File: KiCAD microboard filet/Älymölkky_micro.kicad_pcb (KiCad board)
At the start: 2 copper layers, 36.1 x 21.1 mm, 30 parts, among them U1 nRF52810-QCxx, X1 32MHz Crystal, X1_C1 12pF, X1_C2 12pF, X2 32.768 kHz Crystal, X2_C11 12pF, X2_C12 12pF

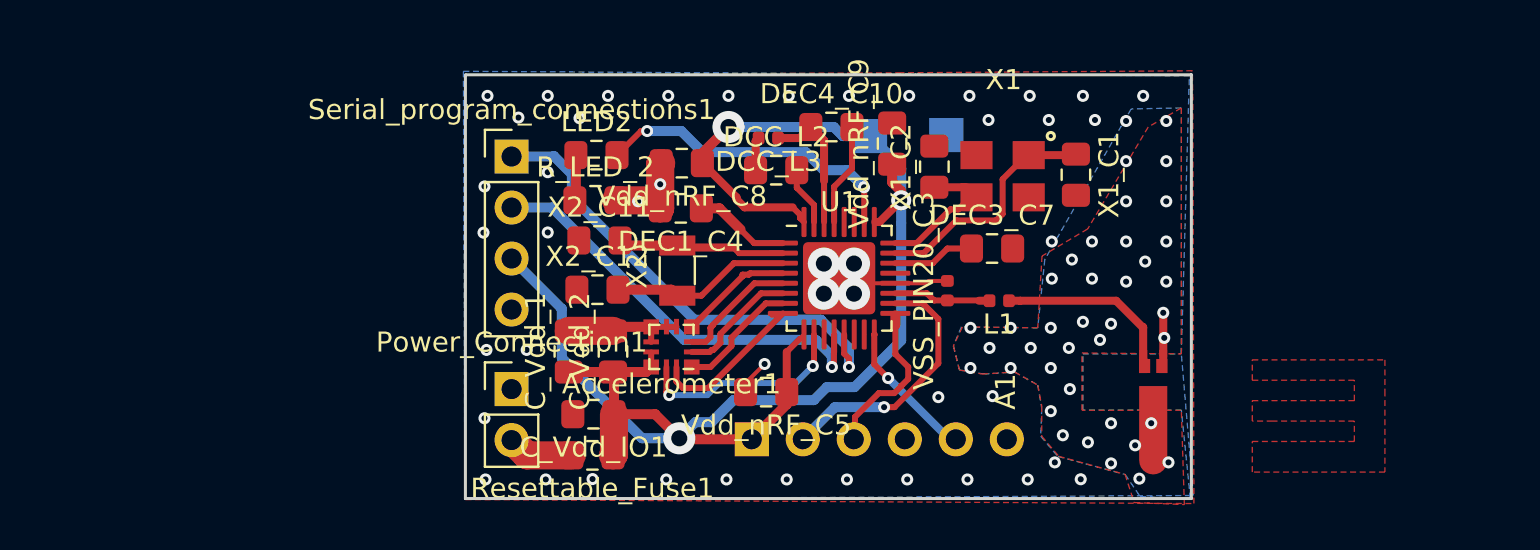
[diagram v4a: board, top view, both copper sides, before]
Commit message: Added battery vias and drew preliminary trace antenna
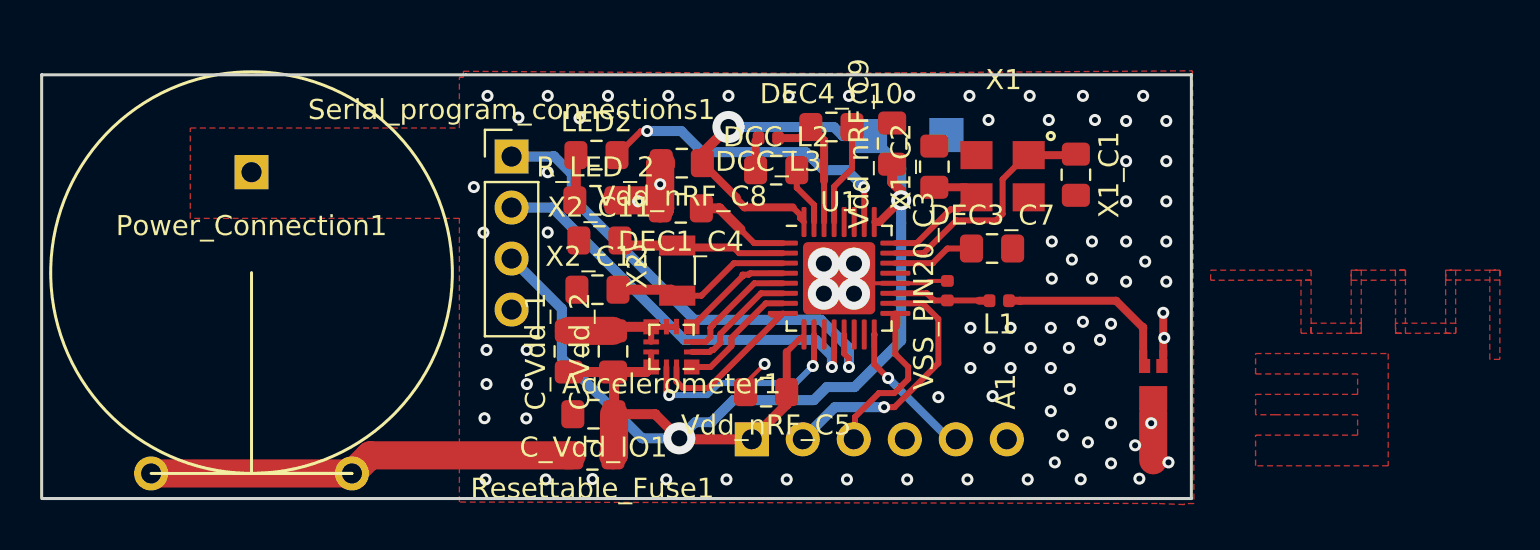
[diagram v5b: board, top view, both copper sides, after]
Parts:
- Power_Connection1: footprint Connector_PinHeader_2.54mm:PinHeader_1x02_P2.54mm_Vertical -> Custom_footprints_alymolkky:PinHeader_1x02_P2.54mm_Vertical
- moved Power_Connection1 14.2 mm to (101.5, 93.7)
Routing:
- net Net-(Power_Connection1-Pad2): track 3.31 -> 21.3 mm
- net Earth: vias 85 -> 88
- added copper zone on F.Cu, net /ANTENNA
- added copper zone on F.Cu, net VDD
- removed copper zone on B.Cu, net Earth
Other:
- board size 36.1 x 21.1 mm -> 57.2 x 21.1 mm

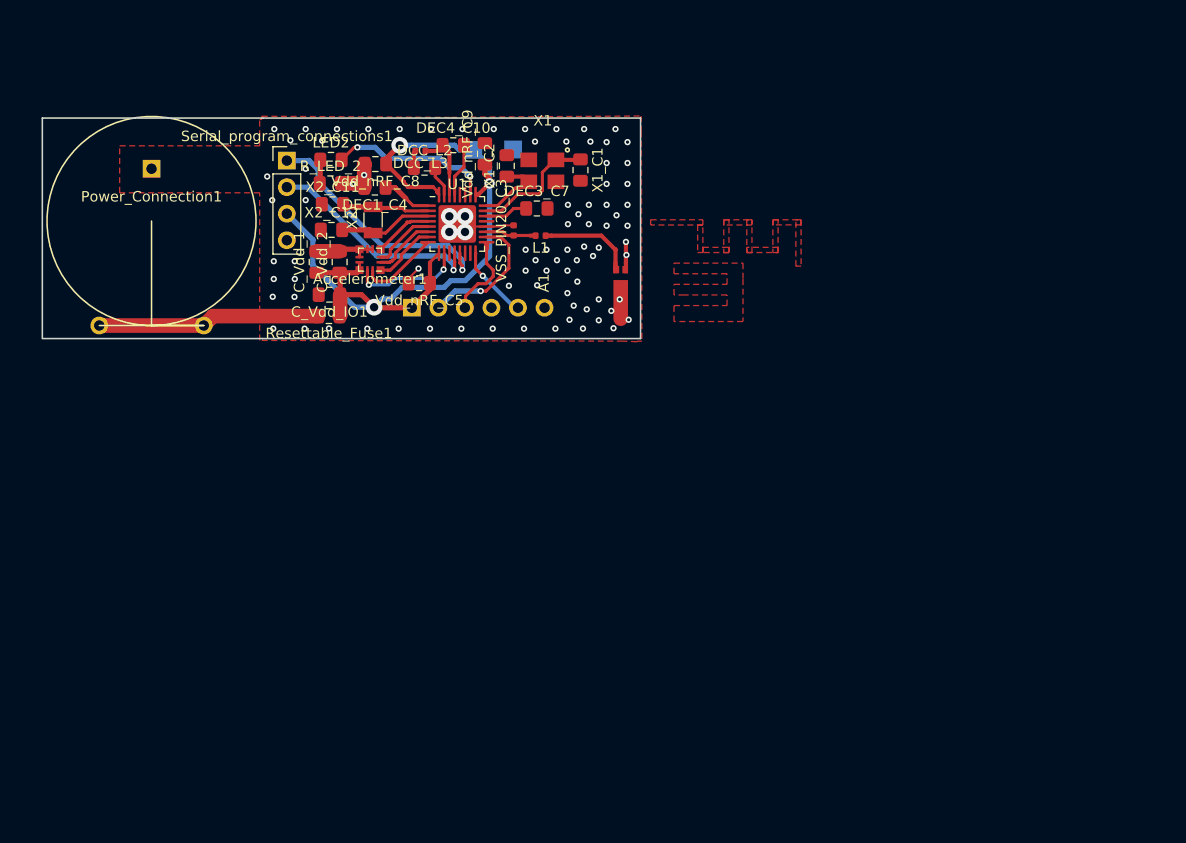
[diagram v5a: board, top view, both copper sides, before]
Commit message: Added new file for order with trace antenna, multiplied the ceramic antenna order pcb for order
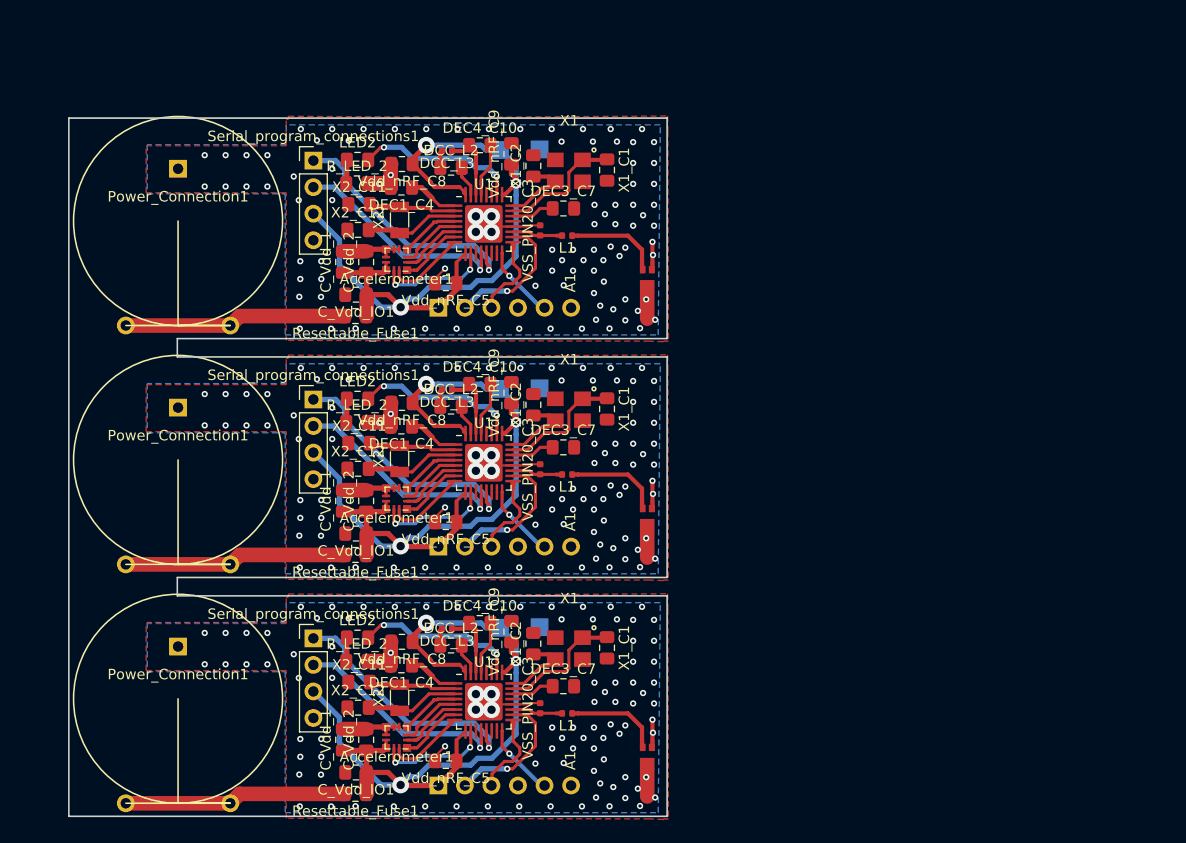
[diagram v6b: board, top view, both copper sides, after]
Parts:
- added A1: ACAG0201-2450-T, ceramic_antenna_footprint:ACAG0201-2450-T, F.Cu at (149.0, 144.8)
- added A1: ACAG0201-2450-T, ceramic_antenna_footprint:ACAG0201-2450-T, F.Cu at (149.0, 121.9)
- added Accelerometer1: LIS2DE12, Custom_footprints_alymolkky:LGA-12_2x2mm_P0.5mm, F.Cu at (125.0, 143.1)
- added Accelerometer1: LIS2DE12, Custom_footprints_alymolkky:LGA-12_2x2mm_P0.5mm, F.Cu at (125.0, 120.3)
- added C_Vdd_1: 100uF, Capacitor_SMD:C_0805_2012Metric_Pad1.15x1.40mm_HandSolder, F.Cu at (119.9, 143.3)
- added C_Vdd_1: 100uF, Capacitor_SMD:C_0805_2012Metric_Pad1.15x1.40mm_HandSolder, F.Cu at (119.9, 120.5)
- added C_Vdd_2: 10uF, Capacitor_SMD:C_0805_2012Metric_Pad1.15x1.40mm_HandSolder, F.Cu at (122.1, 143.3)
- added C_Vdd_2: 10uF, Capacitor_SMD:C_0805_2012Metric_Pad1.15x1.40mm_HandSolder, F.Cu at (122.1, 120.5)
- added C_Vdd_IO1: 100nF, Capacitor_SMD:C_0805_2012Metric_Pad1.15x1.40mm_HandSolder, F.Cu at (121.1, 146.5)
- added C_Vdd_IO1: 100nF, Capacitor_SMD:C_0805_2012Metric_Pad1.15x1.40mm_HandSolder, F.Cu at (121.1, 123.6)
- added DCC_L2: 10uH, Capacitor_SMD:C_0805_2012Metric_Pad1.15x1.40mm_HandSolder, F.Cu at (130.2, 134.3)
- added DCC_L2: 10uH, Capacitor_SMD:C_0805_2012Metric_Pad1.15x1.40mm_HandSolder, F.Cu at (130.2, 111.5)
- added DCC_L3: 15nH, Capacitor_SMD:C_0402_1005Metric, F.Cu at (129.8, 132.7)
- added DCC_L3: 15nH, Capacitor_SMD:C_0402_1005Metric, F.Cu at (129.8, 109.9)
- added DEC1_C4: 100nF, Capacitor_SMD:C_0805_2012Metric_Pad1.15x1.40mm_HandSolder, F.Cu at (125.5, 136.2)
- added DEC1_C4: 100nF, Capacitor_SMD:C_0805_2012Metric_Pad1.15x1.40mm_HandSolder, F.Cu at (125.5, 113.4)
- added DEC3_C7: 100pF, Capacitor_SMD:C_0805_2012Metric_Pad1.15x1.40mm_HandSolder, F.Cu at (141.0, 138.2)
- added DEC3_C7: 100pF, Capacitor_SMD:C_0805_2012Metric_Pad1.15x1.40mm_HandSolder, F.Cu at (141.0, 115.4)
- added DEC4_C10: 1.0uF, Capacitor_SMD:C_0805_2012Metric_Pad1.15x1.40mm_HandSolder, F.Cu at (133.0, 132.2)
- added DEC4_C10: 1.0uF, Capacitor_SMD:C_0805_2012Metric_Pad1.15x1.40mm_HandSolder, F.Cu at (133.0, 109.3)
- added GND_TP1: Conn_01x01_Male, Connector_PinHeader_2.54mm:PinHeader_1x01_P2.54mm_Vertical, B.Cu at (138.7, 132.6)
- added GND_TP1: Conn_01x01_Male, Connector_PinHeader_2.54mm:PinHeader_1x01_P2.54mm_Vertical, B.Cu at (138.7, 109.7)
- added L1: 3.9nH, Resistor_SMD:R_0402_1005Metric, F.Cu at (141.3, 140.8)
- added L1: 3.9nH, Resistor_SMD:R_0402_1005Metric, F.Cu at (141.3, 118.0)
- added LED2: LED_ALT, Resistor_SMD:R_0805_2012Metric_Pad1.15x1.40mm_HandSolder, F.Cu at (121.3, 133.6)
- added LED2: LED_ALT, Resistor_SMD:R_0805_2012Metric_Pad1.15x1.40mm_HandSolder, F.Cu at (121.3, 110.7)
- added Power_Connection1: Conn_01x02_Female, Custom_footprints_alymolkky:PinHeader_1x02_P2.54mm_Vertical, F.Cu at (104.1, 139.4)
- added Power_Connection1: Conn_01x02_Female, Custom_footprints_alymolkky:PinHeader_1x02_P2.54mm_Vertical, F.Cu at (104.1, 116.6)
- added R_LED_2: 220, Resistor_SMD:R_0805_2012Metric_Pad1.15x1.40mm_HandSolder, F.Cu at (121.2, 135.8)
- added R_LED_2: 220, Resistor_SMD:R_0805_2012Metric_Pad1.15x1.40mm_HandSolder, F.Cu at (121.2, 113.0)
- added Resettable_Fuse1: Polyfuse, Resistor_SMD:R_0805_2012Metric_Pad1.15x1.40mm_HandSolder, F.Cu at (121.1, 148.5)
- added Resettable_Fuse1: Polyfuse, Resistor_SMD:R_0805_2012Metric_Pad1.15x1.40mm_HandSolder, F.Cu at (121.1, 125.7)
- added SWD_connections1: Conn_01x06_Male, Connector_PinHeader_2.54mm:PinHeader_1x06_P2.54mm_Vertical, B.Cu at (129.0, 147.7)
- added SWD_connections1: Conn_01x06_Male, Connector_PinHeader_2.54mm:PinHeader_1x06_P2.54mm_Vertical, B.Cu at (129.0, 124.9)
- added Serial_program_connections1: Conn_01x04_Male, Connector_PinHeader_2.54mm:PinHeader_1x04_P2.54mm_Vertical, F.Cu at (117.0, 133.6)
- added Serial_program_connections1: Conn_01x04_Male, Connector_PinHeader_2.54mm:PinHeader_1x04_P2.54mm_Vertical, F.Cu at (117.0, 110.8)
- added U1: nRF52810-QCxx, Custom_footprints_alymolkky:QFN-32-1EP_5x5mm_P0.5mm_EP3.6x3.6mm, F.Cu at (133.3, 139.7)
- added U1: nRF52810-QCxx, Custom_footprints_alymolkky:QFN-32-1EP_5x5mm_P0.5mm_EP3.6x3.6mm, F.Cu at (133.3, 116.8)
- added VDD_TP1: Conn_01x01_Male, Connector_PinHeader_2.54mm:PinHeader_1x01_P2.54mm_Vertical, B.Cu at (134.9, 132.6)
- added VDD_TP1: Conn_01x01_Male, Connector_PinHeader_2.54mm:PinHeader_1x01_P2.54mm_Vertical, B.Cu at (134.9, 109.8)
- added VSS_PIN20_C3: 0.8pF, Capacitor_SMD:C_0402_1005Metric, F.Cu at (138.7, 140.3)
- added VSS_PIN20_C3: 0.8pF, Capacitor_SMD:C_0402_1005Metric, F.Cu at (138.7, 117.5)
- added Vdd_nRF_C5: 100nF, Capacitor_SMD:C_0805_2012Metric_Pad1.15x1.40mm_HandSolder, F.Cu at (129.7, 145.4)
- added Vdd_nRF_C5: 100nF, Capacitor_SMD:C_0805_2012Metric_Pad1.15x1.40mm_HandSolder, F.Cu at (129.7, 122.5)
- added Vdd_nRF_C8: 100nF, Capacitor_SMD:C_0805_2012Metric_Pad1.15x1.40mm_HandSolder, F.Cu at (125.5, 134.0)
- added Vdd_nRF_C8: 100nF, Capacitor_SMD:C_0805_2012Metric_Pad1.15x1.40mm_HandSolder, F.Cu at (125.5, 111.1)
- added Vdd_nRF_C9: 4.7uF, Capacitor_SMD:C_0805_2012Metric_Pad1.15x1.40mm_HandSolder, F.Cu at (136.0, 133.0)
- added Vdd_nRF_C9: 4.7uF, Capacitor_SMD:C_0805_2012Metric_Pad1.15x1.40mm_HandSolder, F.Cu at (136.0, 110.1)
- added X1: 32MHz Crystal, Custom_footprints_alymolkky:Crystal_3.2x2.5x0.8, F.Cu at (141.5, 134.6)
- added X1: 32MHz Crystal, Custom_footprints_alymolkky:Crystal_3.2x2.5x0.8, F.Cu at (141.5, 111.8)
- added X1_C1: 12pF, Capacitor_SMD:C_0805_2012Metric_Pad1.15x1.40mm_HandSolder, F.Cu at (145.1, 134.5)
- added X1_C1: 12pF, Capacitor_SMD:C_0805_2012Metric_Pad1.15x1.40mm_HandSolder, F.Cu at (145.1, 111.7)
- added X1_C2: 12pF, Capacitor_SMD:C_0805_2012Metric_Pad1.15x1.40mm_HandSolder, F.Cu at (138.1, 134.1)
- added X1_C2: 12pF, Capacitor_SMD:C_0805_2012Metric_Pad1.15x1.40mm_HandSolder, F.Cu at (138.1, 111.3)
- added X2: 32.768 kHz Crystal, Crystal:Crystal_SMD_3215-2Pin_3.2x1.5mm, F.Cu at (125.3, 139.3)
- added X2: 32.768 kHz Crystal, Crystal:Crystal_SMD_3215-2Pin_3.2x1.5mm, F.Cu at (125.3, 116.5)
- added X2_C11: 12pF, Capacitor_SMD:C_0805_2012Metric_Pad1.15x1.40mm_HandSolder, F.Cu at (121.4, 137.8)
- added X2_C11: 12pF, Capacitor_SMD:C_0805_2012Metric_Pad1.15x1.40mm_HandSolder, F.Cu at (121.4, 115.0)
- added X2_C12: 12pF, Capacitor_SMD:C_0805_2012Metric_Pad1.15x1.40mm_HandSolder, F.Cu at (121.3, 140.3)
- added X2_C12: 12pF, Capacitor_SMD:C_0805_2012Metric_Pad1.15x1.40mm_HandSolder, F.Cu at (121.3, 117.4)
- moved A1 2.54 mm to (149.0, 99.0)
- moved VSS_PIN20_C3 2.54 mm to (138.7, 94.6)
- moved Vdd_nRF_C9 2.54 mm to (136.0, 87.3)
- moved X1 2.54 mm to (141.5, 88.9)
- moved Accelerometer1 2.54 mm to (125.0, 97.4)
- moved C_Vdd_1 2.54 mm to (119.9, 97.6)
- moved C_Vdd_2 2.54 mm to (122.1, 97.6)
- moved DCC_L2 2.54 mm to (130.2, 88.6)
- moved DEC1_C4 2.54 mm to (125.5, 90.5)
- moved LED2 2.54 mm to (121.3, 87.8)
- moved Power_Connection1 2.54 mm to (104.1, 93.7)
- moved R_LED_2 2.54 mm to (121.2, 90.1)
- moved SWD_connections1 2.54 mm to (129.0, 102.0)
- moved Serial_program_connections1 2.54 mm to (117.0, 87.9)
- moved Vdd_nRF_C5 2.54 mm to (129.7, 99.7)
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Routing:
- net VDD: track 80.3 -> 241.0 mm, vias 3 -> 9
- net Earth: track 28.5 -> 85.6 mm, vias 88 -> 288
- net /~TX0: track 26.5 -> 79.4 mm, vias 1 -> 3
- net Net-(Power_Connection1-Pad2): track 21.3 -> 64.0 mm
- net /~RX1: track 21.2 -> 63.6 mm, vias 1 -> 3
- net Net-(LED2-Pad2): track 15.7 -> 47.1 mm, vias 2 -> 6
- net /~SWDIO: track 13.0 -> 39.0 mm, vias 1 -> 3
- net Net-(U1-Pad23): track 12.0 -> 35.9 mm
- net /~INT2: track 11.0 -> 33.0 mm, vias 2 -> 6
- net Net-(U1-Pad3): track 9.41 -> 28.2 mm
- net /ANTENNA: track 8.96 -> 26.9 mm
- net /~SWDCLK: track 8.33 -> 25.0 mm
- net /~INT1: track 8.30 -> 24.9 mm
- net Net-(U1-Pad2): track 8.08 -> 24.2 mm
- net Net-(U1-Pad24): track 7.54 -> 22.6 mm
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- added copper zone on B.Cu, net Earth
- removed copper zone on F.Cu, net (none)
- removed copper zone on F.Cu, net /ANTENNA
- removed copper zone on F.Cu, net VDD
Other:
- board size 57.2 x 21.1 mm -> 57.2 x 66.8 mm
